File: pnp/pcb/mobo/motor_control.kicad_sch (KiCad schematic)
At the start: 0 parts

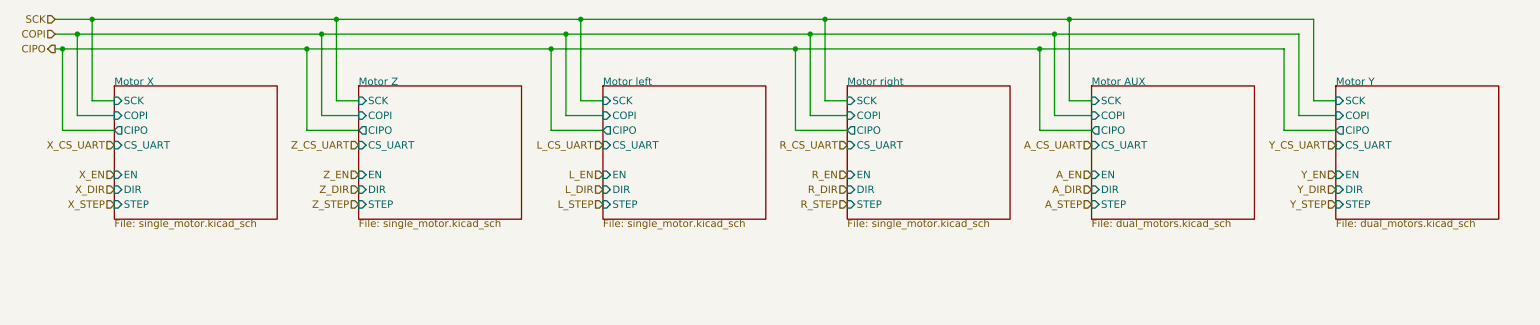
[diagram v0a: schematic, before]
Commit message: another huge chunk of work on rev04 of the mobo. breaks out diag and index pin for TMC2209 sensorless homing. reduces unique part count by consolidating resistor values where possible. replaces full ADC pipeline with monolithic I2C vacuum sensor and an I2C multiplexer due to address collision issues with two sensors. adds solder selectable jumpers for selecting whether an axis uses switch or TMC homing. redoes lots of routing of the SPI lines up to the stepper drivers.
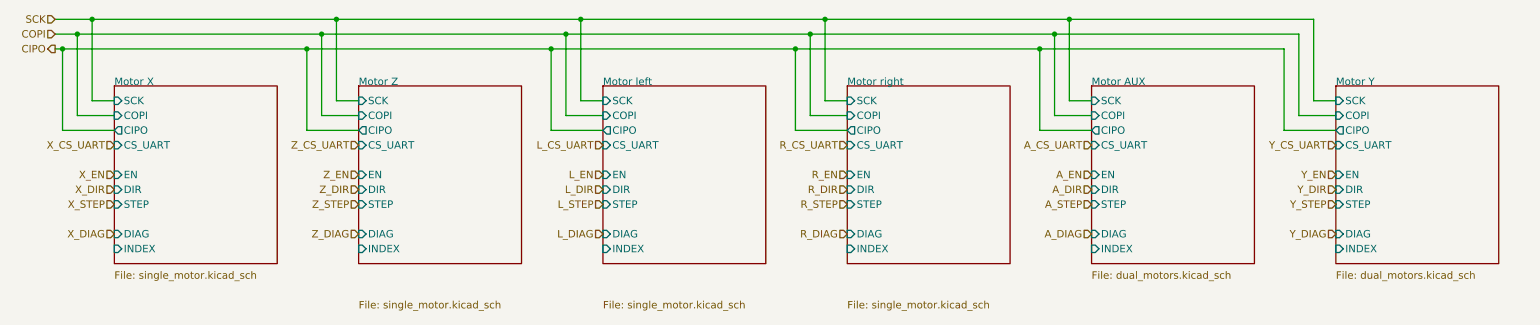
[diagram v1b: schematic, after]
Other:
- sheet Motor AUX ports: added DIAG, INDEX; removed none
- sheet Motor X ports: added DIAG, INDEX; removed none
- sheet Motor Y ports: added DIAG, INDEX; removed none
- sheet Motor Z ports: added DIAG, INDEX; removed none
- sheet Motor left ports: added DIAG, INDEX; removed none
- sheet Motor right ports: added DIAG, INDEX; removed none
- company: (none) -> Opulo
- title: Motors -> LumenPnP Motherboard
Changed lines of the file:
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@@
   (paper "A4")
   (title_block
-    (title "Motors")
+    (title "LumenPnP Motherboard")
     (date "2022-03-29")
     (rev "003")
+    (company "Opulo")
   )
   (junction (at 114.3 81.28) (diameter 0) (color 0 0 0 0)
@@
     (effects (font (size 1.27 1.27)) (justify right))
   )
+  (hierarchical_label "Z_DIAG" (shape input) (at 78.74 115.57 180)
+    (effects (font (size 1.27 1.27)) (justify right))
+  )
   (hierarchical_label "Z_CS_UART" (shape input) (at 78.74 100.33 180)
     (effects (font (size 1.27 1.27)) (justify right))
@@
     (effects (font (size 1.27 1.27)) (justify right))
   )
+  (hierarchical_label "A_DIAG" (shape input) (at 204.47 115.57 180)
+    (effects (font (size 1.27 1.27)) (justify right))
+  )
   (hierarchical_label "Z_STEP" (shape input) (at 78.74 110.49 180)
     (effects (font (size 1.27 1.27)) (justify right))
@@
     (effects (font (size 1.27 1.27)) (justify right))
   )
+  (hierarchical_label "L_DIAG" (shape input) (at 120.65 115.57 180)
+    (effects (font (size 1.27 1.27)) (justify right))
+  )
   (hierarchical_label "L_CS_UART" (shape input) (at 120.65 100.33 180)
     (effects (font (size 1.27 1.27)) (justify right))
@@
     (effects (font (size 1.27 1.27)) (justify right))
   )
+  (hierarchical_label "X_DIAG" (shape input) (at 36.83 115.57 180)
+    (effects (font (size 1.27 1.27)) (justify right))
+  )
   (hierarchical_label "R_EN" (shape input) (at 162.56 105.41 180)
     (effects (font (size 1.27 1.27)) (justify right))
   )
+  (hierarchical_label "Y_DIAG" (shape input) (at 246.38 115.57 180)
+    (effects (font (size 1.27 1.27)) (justify right))
+  )
   (hierarchical_label "R_CS_UART" (shape input) (at 162.56 100.33 180)
     (effects (font (size 1.27 1.27)) (justify right))
@@
     (effects (font (size 1.27 1.27)) (justify right))
   )
-  (sheet (at 36.83 90.17) (size 27.94 22.86)
+  (hierarchical_label "R_DIAG" (shape input) (at 162.56 115.57 180)
+    (effects (font (size 1.27 1.27)) (justify right))
+  )
+  (sheet (at 36.83 90.17) (size 27.94 30.48)
     (stroke (width 0) (type solid) (color 0 0 0 0))
     (fill (color 0 0 0 0.0000))
@@
       (effects (font (size 1.27 1.27)) (justify left bottom))
     )
-    (property "Sheet file" "single_motor.kicad_sch" (id 1) (at 36.83 113.03 0)
+    (property "Sheet file" "single_motor.kicad_sch" (id 1) (at 36.83 121.92 0)
       (effects (font (size 1.27 1.27)) (justify left top))
     )
@@
       (effects (font (size 1.27 1.27)) (justify left))
     )
-  )
-  (sheet (at 204.47 90.17) (size 27.94 22.86)
+    (pin "DIAG" input (at 36.83 115.57 180)
+      (effects (font (size 1.27 1.27)) (justify left))
+    )
+    (pin "INDEX" input (at 36.83 118.11 180)
+      (effects (font (size 1.27 1.27)) (justify left))
+    )
+  )
+  (sheet (at 204.47 90.17) (size 27.94 30.48)
     (stroke (width 0) (type solid) (color 0 0 0 0))
     (fill (color 0 0 0 0.0000))
@@
       (effects (font (size 1.27 1.27)) (justify left bottom))
     )
-    (property "Sheet file" "dual_motors.kicad_sch" (id 1) (at 204.47 113.03 0)
+    (property "Sheet file" "dual_motors.kicad_sch" (id 1) (at 204.47 121.92 0)
       (effects (font (size 1.27 1.27)) (justify left top))
     )
@@
       (effects (font (size 1.27 1.27)) (justify left))
     )
-  )
-  (sheet (at 78.74 90.17) (size 27.94 22.86)
+    (pin "INDEX" input (at 204.47 118.11 180)
+      (effects (font (size 1.27 1.27)) (justify left))
+    )
+    (pin "DIAG" input (at 204.47 115.57 180)
+      (effects (font (size 1.27 1.27)) (justify left))
+    )
+  )
+  (sheet (at 78.74 90.17) (size 27.94 30.48)
     (stroke (width 0) (type solid) (color 0 0 0 0))
     (fill (color 0 0 0 0.0000))
@@
       (effects (font (size 1.27 1.27)) (justify left bottom))
     )
-    (property "Sheet file" "single_motor.kicad_sch" (id 1) (at 78.74 113.03 0)
+    (property "Sheet file" "single_motor.kicad_sch" (id 1) (at 78.74 127 0)
       (effects (font (size 1.27 1.27)) (justify left top))
     )
@@
       (effects (font (size 1.27 1.27)) (justify left))
     )
-  )
-  (sheet (at 162.56 90.17) (size 27.94 22.86)
+    (pin "DIAG" input (at 78.74 115.57 180)
+      (effects (font (size 1.27 1.27)) (justify left))
+    )
+    (pin "INDEX" input (at 78.74 118.11 180)
+      (effects (font (size 1.27 1.27)) (justify left))
+    )
+  )
+  (sheet (at 162.56 90.17) (size 27.94 30.48)
     (stroke (width 0) (type solid) (color 0 0 0 0))
     (fill (color 0 0 0 0.0000))
@@
       (effects (font (size 1.27 1.27)) (justify left bottom))
     )
-    (property "Sheet file" "single_motor.kicad_sch" (id 1) (at 162.56 113.03 0)
+    (property "Sheet file" "single_motor.kicad_sch" (id 1) (at 162.56 127 0)
       (effects (font (size 1.27 1.27)) (justify left top))
     )
@@
       (effects (font (size 1.27 1.27)) (justify left))
     )
-  )
-  (sheet (at 246.38 90.17) (size 27.94 22.86)
+    (pin "INDEX" input (at 162.56 118.11 180)
+      (effects (font (size 1.27 1.27)) (justify left))
+    )
+    (pin "DIAG" input (at 162.56 115.57 180)
+      (effects (font (size 1.27 1.27)) (justify left))
+    )
+  )
+  (sheet (at 246.38 90.17) (size 27.94 30.48)
     (stroke (width 0) (type solid) (color 0 0 0 0))
     (fill (color 0 0 0 0.0000))
@@
       (effects (font (size 1.27 1.27)) (justify left bottom))
     )
-    (property "Sheet file" "dual_motors.kicad_sch" (id 1) (at 246.38 113.03 0)
+    (property "Sheet file" "dual_motors.kicad_sch" (id 1) (at 246.38 121.92 0)
       (effects (font (size 1.27 1.27)) (justify left top))
     )
@@
       (effects (font (size 1.27 1.27)) (justify left))
     )
-  )
-  (sheet (at 120.65 90.17) (size 27.94 22.86)
+    (pin "INDEX" input (at 246.38 118.11 180)
+      (effects (font (size 1.27 1.27)) (justify left))
+    )
+    (pin "DIAG" input (at 246.38 115.57 180)
+      (effects (font (size 1.27 1.27)) (justify left))
+    )
+  )
+  (sheet (at 120.65 90.17) (size 27.94 30.48)
     (stroke (width 0) (type solid) (color 0 0 0 0))
     (fill (color 0 0 0 0.0000))
@@
       (effects (font (size 1.27 1.27)) (justify left bottom))
     )
-    (property "Sheet file" "single_motor.kicad_sch" (id 1) (at 120.65 113.03 0)
+    (property "Sheet file" "single_motor.kicad_sch" (id 1) (at 120.65 127 0)
       (effects (font (size 1.27 1.27)) (justify left top))
     )
@@
       (effects (font (size 1.27 1.27)) (justify left))
     )
+    (pin "INDEX" input (at 120.65 118.11 180)
+      (effects (font (size 1.27 1.27)) (justify left))
+    )
+    (pin "DIAG" input (at 120.65 115.57 180)
+      (effects (font (size 1.27 1.27)) (justify left))
+    )
